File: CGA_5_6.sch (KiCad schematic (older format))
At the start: 34 parts, among them Q1 2N3904, U13 74LS08, U14 74LS32, U15 74LS00, U20 74LS04, U21 74LS174, U24 74LS244, U41 74LS08, U42 74LS86, U43 74S74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

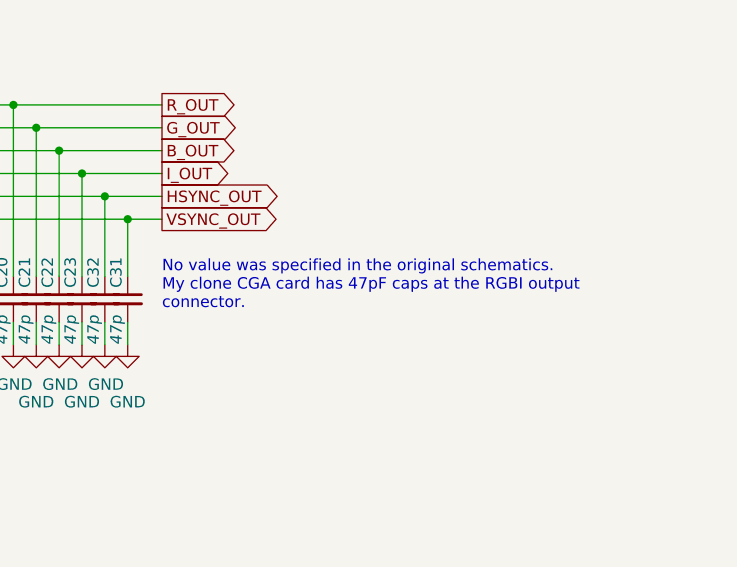
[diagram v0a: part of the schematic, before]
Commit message: Update note on caps at the RGBI connector
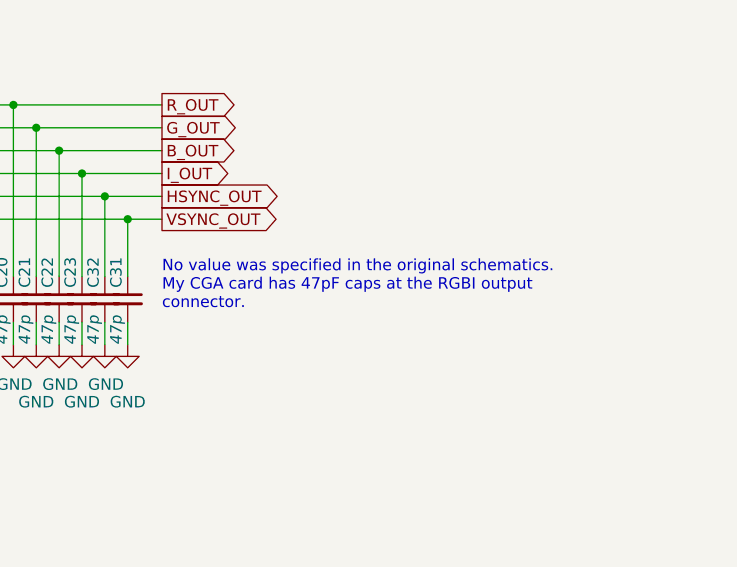
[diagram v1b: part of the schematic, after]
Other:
- note added: "No value was specified in the original schematics.\nMy CGA card has 47pF caps at the RGBI output\nconnector."
- note removed: "No value was specified in the original schematics.\nMy clone CGA card has 47pF caps at the RGBI output\nconnector."
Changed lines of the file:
@@
 $EndComp
 Text Notes 11850 8200 0    50   ~ 0
-No value was specified in the original schematics.\nMy clone CGA card has 47pF caps at the RGBI output\nconnector.
+No value was specified in the original schematics.\nMy CGA card has 47pF caps at the RGBI output\nconnector.
 Wire Wire Line
 	10600 7900 10600 8000

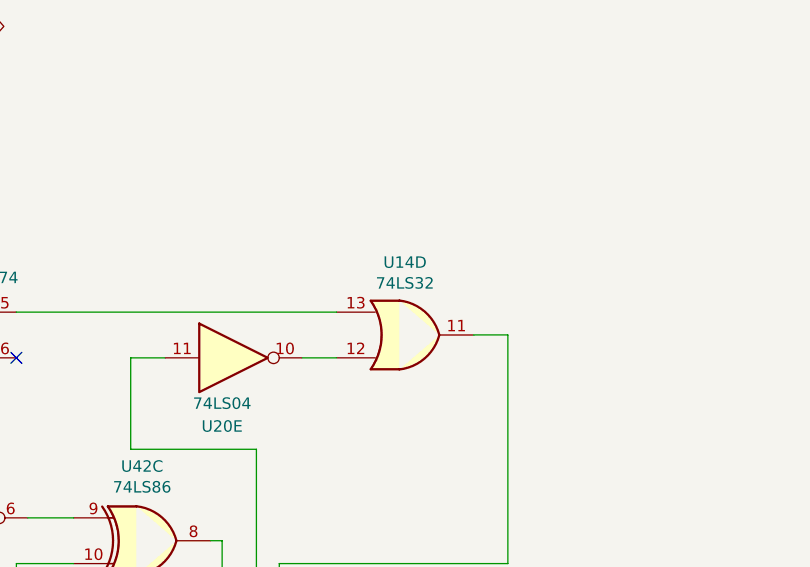
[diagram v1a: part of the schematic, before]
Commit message: Reorganize space between ICs
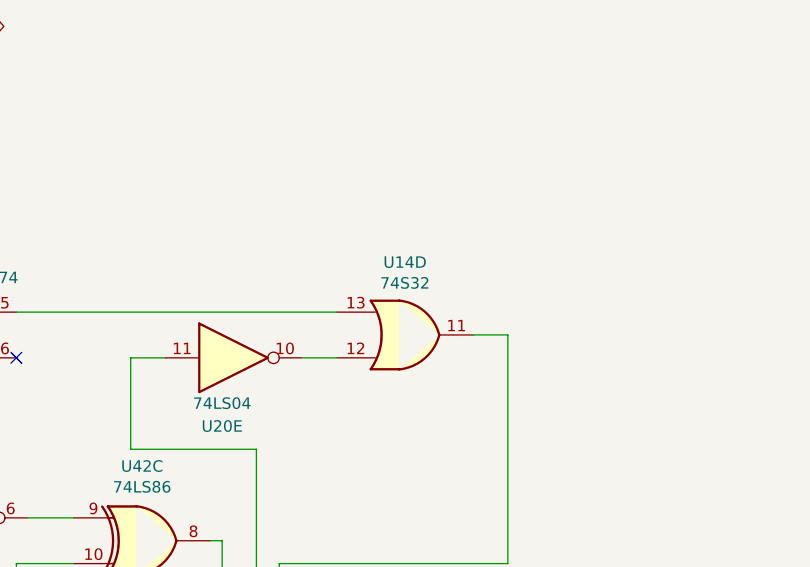
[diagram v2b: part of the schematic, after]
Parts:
- U14: value 74LS32 -> 74S32
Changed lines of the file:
@@
 AR Path="/60463CF3/6401699A" Ref="U14"  Part="4"
 F 0 "U14" H 7200 2933 50  0000 C CNN
-F 1 "74LS32" H 7200 3024 50  0000 C CNN
+F 1 "74S32" H 7200 3024 50  0000 C CNN
 F 2 "Package_DIP:DIP-14_W7.62mm_LongPads" H 7200 3250 50  0001 C CNN
 F 3 "http://www.ti.com/lit/gpn/sn74LS32" H 7200 3250 50  0001 C CNN

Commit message: Changed footprints, moving components
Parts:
- U13, U14, U15, U20, U41, U42, U43, U44, U62, U64, U65, U68: footprint Package_DIP:DIP-14_W7.62mm_LongPads -> Package_DIP:DIP-14_W7.62mm
- U21, U45, U63: footprint Package_DIP:DIP-16_W7.62mm_LongPads -> Package_DIP:DIP-16_W7.62mm
- U24, U67: footprint Package_DIP:DIP-20_W7.62mm_LongPads -> Package_DIP:DIP-20_W7.62mm
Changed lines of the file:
@@
 F 0 "U20" H 1550 550 50  0000 C CNN
 F 1 "74LS04" H 1550 650 50  0000 C CNN
-F 2 "Package_DIP:DIP-14_W7.62mm_LongPads" H 1600 850 50  0001 C CNN
+F 2 "Package_DIP:DIP-14_W7.62mm" H 1600 850 50  0001 C CNN
 F 3 "http://www.ti.com/lit/gpn/sn74LS04" H 1600 850 50  0001 C CNN
 	2    1600 850
@@
 F 0 "U13" H 6200 633 50  0000 C CNN
 F 1 "74LS08" H 6200 724 50  0000 C CNN
-F 2 "Package_DIP:DIP-14_W7.62mm_LongPads" H 6200 950 50  0001 C CNN
+F 2 "Package_DIP:DIP-14_W7.62mm" H 6200 950 50  0001 C CNN
 F 3 "http://www.ti.com/lit/gpn/sn74LS08" H 6200 950 50  0001 C CNN
 	1    6200 950
@@
 F 0 "U20" H 1600 1200 50  0000 C CNN
 F 1 "74LS04" H 1600 1300 50  0000 C CNN
-F 2 "Package_DIP:DIP-14_W7.62mm_LongPads" H 1650 1500 50  0001 C CNN
+F 2 "Package_DIP:DIP-14_W7.62mm" H 1650 1500 50  0001 C CNN
 F 3 "http://www.ti.com/lit/gpn/sn74LS04" H 1650 1500 50  0001 C CNN
 	1    1650 1500
@@
 F 0 "U21" H 2800 2450 50  0000 C CNN
 F 1 "74LS174" H 3250 2450 50  0000 C CNN
-F 2 "Package_DIP:DIP-16_W7.62mm_LongPads" H 3050 1900 50  0001 C CNN
+F 2 "Package_DIP:DIP-16_W7.62mm" H 3050 1900 50  0001 C CNN
 F 3 "http://www.ti.com/lit/gpn/sn74LS174" H 3050 1900 50  0001 C CNN
 	1    3050 1900
@@
 F 0 "U15" H 5050 1450 50  0000 C CNN
 F 1 "74LS00" H 5400 1450 50  0000 C CNN
-F 2 "Package_DIP:DIP-14_W7.62mm_LongPads" H 5300 1250 50  0001 C CNN
+F 2 "Package_DIP:DIP-14_W7.62mm" H 5300 1250 50  0001 C CNN
 F 3 "http://www.ti.com/lit/gpn/sn74ls00" H 5300 1250 50  0001 C CNN
 	1    5300 1250
@@
 F 0 "U64" H 2350 4500 50  0000 C CNN
 F 1 "74LS164" H 2800 4500 50  0000 C CNN
-F 2 "Package_DIP:DIP-14_W7.62mm_LongPads" H 3500 3750 50  0001 C CNN
+F 2 "Package_DIP:DIP-14_W7.62mm" H 3500 3750 50  0001 C CNN
 F 3 "https://assets.nexperia.com/documents/data-sheet/74HC_HCT164.pdf" H 3500 3750 50  0001 C CNN
 	1    2600 4050
@@
 F 0 "U43" H 5050 3500 50  0000 C CNN
 F 1 "74S74" H 5400 3500 50  0000 C CNN
-F 2 "Package_DIP:DIP-14_W7.62mm_LongPads" H 5200 3250 50  0001 C CNN
+F 2 "Package_DIP:DIP-14_W7.62mm" H 5200 3250 50  0001 C CNN
 F 3 "74xx/74hc_hct74.pdf" H 5200 3250 50  0001 C CNN
 	1    5200 3250
@@
 F 0 "U15" H 5250 4375 50  0000 C CNN
 F 1 "74LS00" H 5250 4284 50  0000 C CNN
-F 2 "Package_DIP:DIP-14_W7.62mm_LongPads" H 5250 4050 50  0001 C CNN
+F 2 "Package_DIP:DIP-14_W7.62mm" H 5250 4050 50  0001 C CNN
 F 3 "http://www.ti.com/lit/gpn/sn74ls00" H 5250 4050 50  0001 C CNN
 	2    5250 4050
@@
 F 0 "U42" H 6050 4475 50  0000 C CNN
 F 1 "74LS86" H 6050 4384 50  0000 C CNN
-F 2 "Package_DIP:DIP-14_W7.62mm_LongPads" H 6050 4150 50  0001 C CNN
+F 2 "Package_DIP:DIP-14_W7.62mm" H 6050 4150 50  0001 C CNN
 F 3 "74xx/74ls86.pdf" H 6050 4150 50  0001 C CNN
 	3    6050 4150
@@
 F 0 "U14" H 7200 2933 50  0000 C CNN
 F 1 "74S32" H 7200 3024 50  0000 C CNN
-F 2 "Package_DIP:DIP-14_W7.62mm_LongPads" H 7200 3250 50  0001 C CNN
+F 2 "Package_DIP:DIP-14_W7.62mm" H 7200 3250 50  0001 C CNN
 F 3 "http://www.ti.com/lit/gpn/sn74LS32" H 7200 3250 50  0001 C CNN
 	4    7200 3250
@@
 F 0 "U20" H 6400 3050 50  0000 C CNN
 F 1 "74LS04" H 6400 3150 50  0000 C CNN
-F 2 "Package_DIP:DIP-14_W7.62mm_LongPads" H 6450 3350 50  0001 C CNN
+F 2 "Package_DIP:DIP-14_W7.62mm" H 6450 3350 50  0001 C CNN
 F 3 "http://www.ti.com/lit/gpn/sn74LS04" H 6450 3350 50  0001 C CNN
 	5    6450 3350
@@
 F 0 "U63" H 2350 6900 50  0000 C CNN
 F 1 "74LS175" H 2800 6900 50  0000 C CNN
-F 2 "Package_DIP:DIP-16_W7.62mm_LongPads" H 2600 6350 50  0001 C CNN
+F 2 "Package_DIP:DIP-16_W7.62mm" H 2600 6350 50  0001 C CNN
 F 3 "http://www.ti.com/lit/gpn/sn74LS175" H 2600 6350 50  0001 C CNN
 	1    2600 6350
@@
 F 0 "U41" H 4550 5950 50  0000 C CNN
 F 1 "74LS08" H 4600 6150 50  0000 C CNN
-F 2 "Package_DIP:DIP-14_W7.62mm_LongPads" H 4300 6050 50  0001 C CNN
+F 2 "Package_DIP:DIP-14_W7.62mm" H 4300 6050 50  0001 C CNN
 F 3 "http://www.ti.com/lit/gpn/sn74LS08" H 4300 6050 50  0001 C CNN
 	3    4300 6050
@@
 F 0 "U42" H 5400 5975 50  0000 C CNN
 F 1 "74LS86" H 5400 5884 50  0000 C CNN
-F 2 "Package_DIP:DIP-14_W7.62mm_LongPads" H 5400 5650 50  0001 C CNN
+F 2 "Package_DIP:DIP-14_W7.62mm" H 5400 5650 50  0001 C CNN
 F 3 "74xx/74ls86.pdf" H 5400 5650 50  0001 C CNN
 	2    5400 5650
@@
 F 0 "U20" H 6350 5350 50  0000 C CNN
 F 1 "74LS04" H 6350 5450 50  0000 C CNN
-F 2 "Package_DIP:DIP-14_W7.62mm_LongPads" H 6400 5650 50  0001 C CNN
+F 2 "Package_DIP:DIP-14_W7.62mm" H 6400 5650 50  0001 C CNN
 F 3 "http://www.ti.com/lit/gpn/sn74LS04" H 6400 5650 50  0001 C CNN
 	6    6400 5650
@@
 F 0 "U62" H 9100 1317 50  0000 C CNN
 F 1 "74LS125" H 9100 1226 50  0000 C CNN
-F 2 "Package_DIP:DIP-14_W7.62mm_LongPads" H 9100 1000 50  0001 C CNN
+F 2 "Package_DIP:DIP-14_W7.62mm" H 9100 1000 50  0001 C CNN
 F 3 "http://www.ti.com/lit/gpn/sn74LS125" H 9100 1000 50  0001 C CNN
 	3    9100 1000
@@
 F 0 "U62" H 9900 1317 50  0000 C CNN
 F 1 "74LS125" H 9900 1226 50  0000 C CNN
-F 2 "Package_DIP:DIP-14_W7.62mm_LongPads" H 9900 1000 50  0001 C CNN
+F 2 "Package_DIP:DIP-14_W7.62mm" H 9900 1000 50  0001 C CNN
 F 3 "http://www.ti.com/lit/gpn/sn74LS125" H 9900 1000 50  0001 C CNN
 	4    9900 1000
@@
 F 0 "U67" H 9350 8450 50  0000 C CNN
 F 1 "74LS244" H 9750 8450 50  0000 C CNN
-F 2 "Package_DIP:DIP-20_W7.62mm_LongPads" H 9550 7800 50  0001 C CNN
+F 2 "Package_DIP:DIP-20_W7.62mm" H 9550 7800 50  0001 C CNN
 F 3 "http://www.ti.com/lit/ds/symlink/sn74ls244.pdf" H 9550 7800 50  0001 C CNN
 	1    9550 7800
@@
 F 0 "U65" H 1400 9075 50  0000 C CNN
 F 1 "74LS02" H 1400 8984 50  0000 C CNN
-F 2 "Package_DIP:DIP-14_W7.62mm_LongPads" H 1400 8750 50  0001 C CNN
+F 2 "Package_DIP:DIP-14_W7.62mm" H 1400 8750 50  0001 C CNN
 F 3 "http://www.ti.com/lit/gpn/sn74ls02" H 1400 8750 50  0001 C CNN
 	3    1400 8750
@@
 F 0 "U68" H 2450 8975 50  0000 C CNN
 F 1 "74LS86" H 2450 8884 50  0000 C CNN
-F 2 "Package_DIP:DIP-14_W7.62mm_LongPads" H 2450 8650 50  0001 C CNN
+F 2 "Package_DIP:DIP-14_W7.62mm" H 2450 8650 50  0001 C CNN
 F 3 "74xx/74ls86.pdf" H 2450 8650 50  0001 C CNN
 	2    2450 8650
@@
 F 0 "U68" H 2300 9350 50  0000 C CNN
 F 1 "74LS86" H 2350 8950 50  0000 C CNN
-F 2 "Package_DIP:DIP-14_W7.62mm_LongPads" H 2350 9150 50  0001 C CNN
+F 2 "Package_DIP:DIP-14_W7.62mm" H 2350 9150 50  0001 C CNN
 F 3 "74xx/74ls86.pdf" H 2350 9150 50  0001 C CNN
 	1    2350 9150
@@
 F 0 "U43" H 1400 10650 50  0000 C CNN
 F 1 "74S74" H 1700 10650 50  0000 C CNN
-F 2 "Package_DIP:DIP-14_W7.62mm_LongPads" H 1550 10400 50  0001 C CNN
+F 2 "Package_DIP:DIP-14_W7.62mm" H 1550 10400 50  0001 C CNN
 F 3 "74xx/74hc_hct74.pdf" H 1550 10400 50  0001 C CNN
 	2    1550 10400
@@
 F 0 "U44" H 2400 10650 50  0000 C CNN
 F 1 "74S74" H 2700 10650 50  0000 C CNN
-F 2 "Package_DIP:DIP-14_W7.62mm_LongPads" H 2550 10400 50  0001 C CNN
+F 2 "Package_DIP:DIP-14_W7.62mm" H 2550 10400 50  0001 C CNN
 F 3 "74xx/74hc_hct74.pdf" H 2550 10400 50  0001 C CNN
 	1    2550 10400
@@
 F 0 "U44" H 3350 10650 50  0000 C CNN
 F 1 "74S74" H 3650 10650 50  0000 C CNN
-F 2 "Package_DIP:DIP-14_W7.62mm_LongPads" H 3500 10400 50  0001 C CNN
+F 2 "Package_DIP:DIP-14_W7.62mm" H 3500 10400 50  0001 C CNN
 F 3 "74xx/74hc_hct74.pdf" H 3500 10400 50  0001 C CNN
 	2    3500 10400
@@
 F 0 "U45" H 5600 9800 50  0000 C CNN
 F 1 "74LS151" H 6050 9800 50  0000 C CNN
-F 2 "Package_DIP:DIP-16_W7.62mm_LongPads" H 5850 9050 50  0001 C CNN
+F 2 "Package_DIP:DIP-16_W7.62mm" H 5850 9050 50  0001 C CNN
 F 3 "http://www.ti.com/lit/gpn/sn74LS151" H 5850 9050 50  0001 C CNN
 	1    5850 9050
@@
 F 0 "U24" H 9450 5800 50  0000 C CNN
 F 1 "74LS244" H 10000 5800 50  0000 C CNN
-F 2 "Package_DIP:DIP-20_W7.62mm_LongPads" H 9750 5900 50  0001 C CNN
+F 2 "Package_DIP:DIP-20_W7.62mm" H 9750 5900 50  0001 C CNN
 F 3 "http://www.ti.com/lit/ds/symlink/sn74ls241.pdf" H 9750 5900 50  0001 C CNN
 	1    9750 5900
@@
 F 0 "U24" H 9450 5450 50  0000 C CNN
 F 1 "74LS244" H 10000 5450 50  0000 C CNN
-F 2 "Package_DIP:DIP-20_W7.62mm_LongPads" H 9750 5550 50  0001 C CNN
+F 2 "Package_DIP:DIP-20_W7.62mm" H 9750 5550 50  0001 C CNN
 F 3 "http://www.ti.com/lit/ds/symlink/sn74ls241.pdf" H 9750 5550 50  0001 C CNN
 	2    9750 5550
@@
 F 0 "U24" H 9450 5100 50  0000 C CNN
 F 1 "74LS244" H 10000 5100 50  0000 C CNN
-F 2 "Package_DIP:DIP-20_W7.62mm_LongPads" H 9750 5200 50  0001 C CNN
+F 2 "Package_DIP:DIP-20_W7.62mm" H 9750 5200 50  0001 C CNN
 F 3 "http://www.ti.com/lit/ds/symlink/sn74ls241.pdf" H 9750 5200 50  0001 C CNN
 	3    9750 5200
@@
 F 0 "U24" H 9450 4750 50  0000 C CNN
 F 1 "74LS244" H 10000 4750 50  0000 C CNN
-F 2 "Package_DIP:DIP-20_W7.62mm_LongPads" H 9750 4850 50  0001 C CNN
+F 2 "Package_DIP:DIP-20_W7.62mm" H 9750 4850 50  0001 C CNN
 F 3 "http://www.ti.com/lit/ds/symlink/sn74ls241.pdf" H 9750 4850 50  0001 C CNN
 	4    9750 4850
